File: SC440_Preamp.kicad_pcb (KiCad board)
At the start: 2 copper layers, 30 x 35 mm, 20 parts, among them J1 JST-XH 1x04 TO DIGITAL BOARD, J2 ANALOG BOARD, U1 OPA1678IDR

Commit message: some minor modifications
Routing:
- net /VCC_A: track 34.8 -> 32.4 mm
- net +5V: track 17.0 -> 15.9 mm

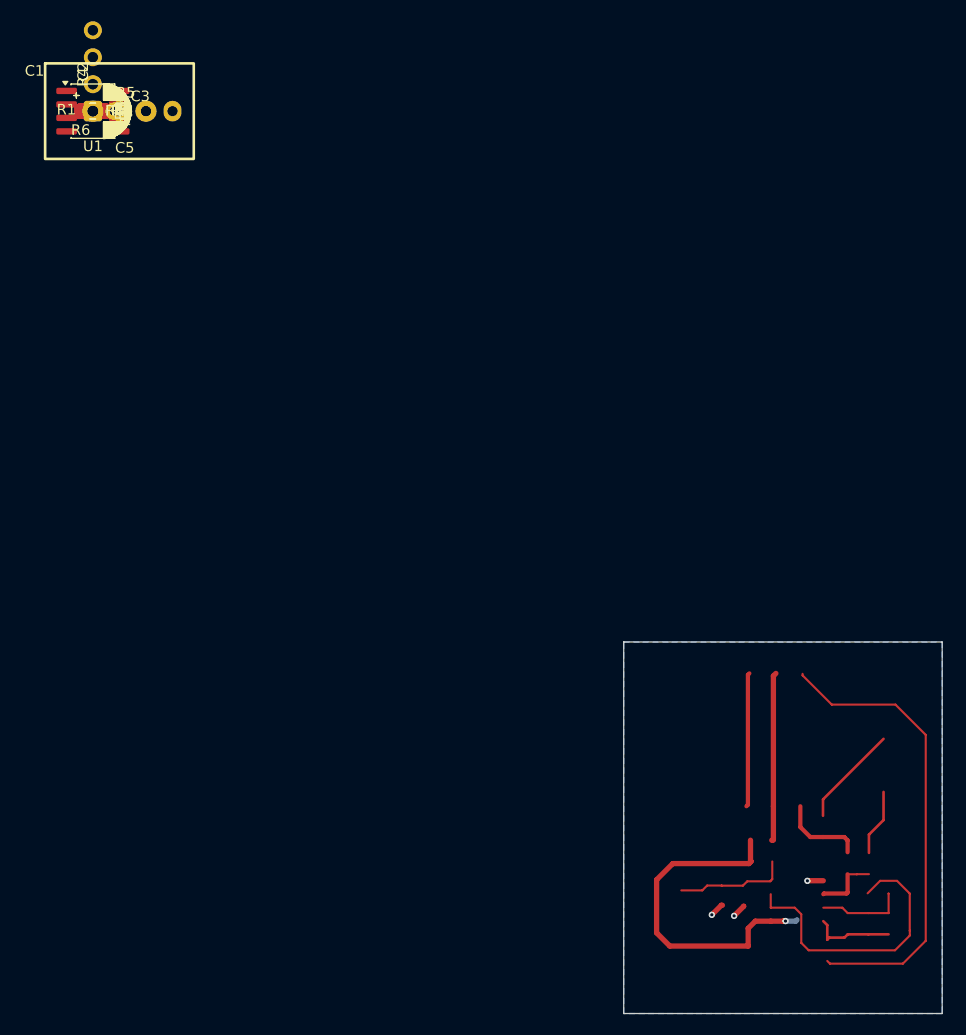
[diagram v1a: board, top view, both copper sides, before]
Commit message: add input and output filter
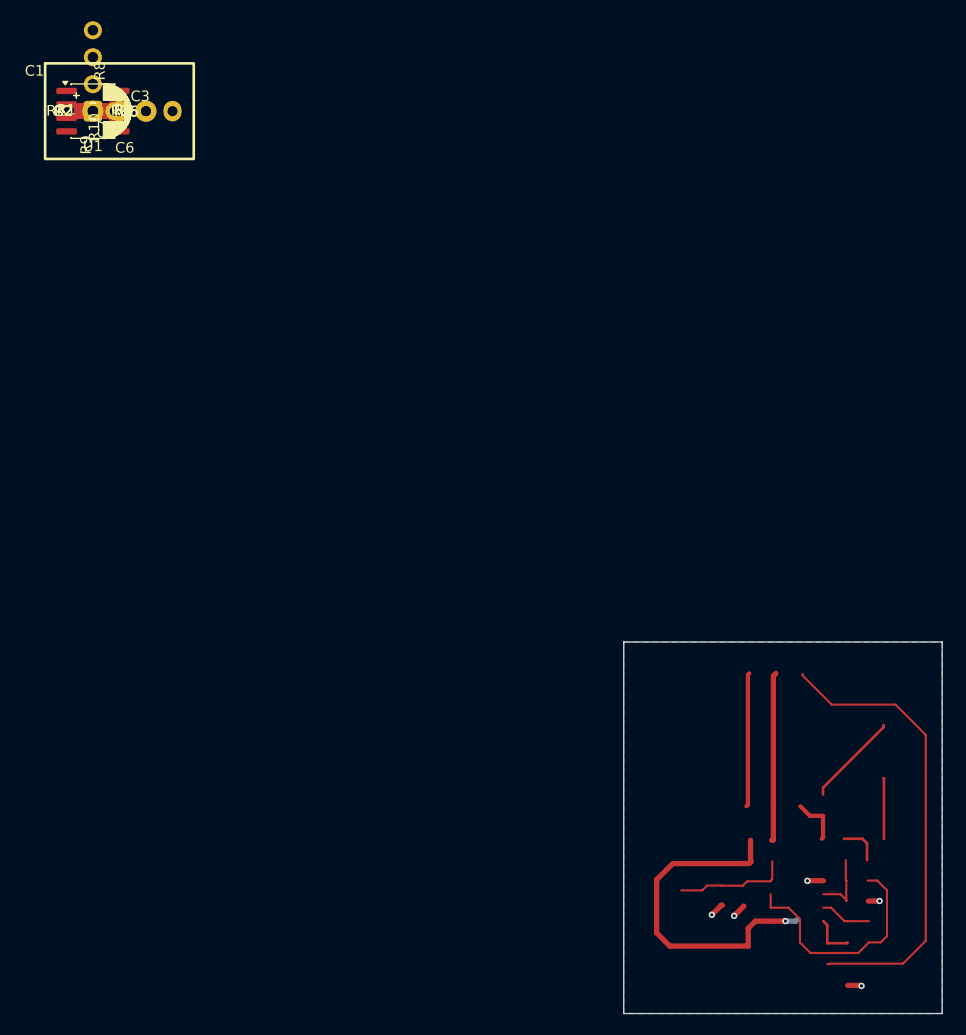
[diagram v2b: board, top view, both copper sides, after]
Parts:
- removed the R8 at (0.00, 0.00)
- removed the R9 at (0.00, 0.00)
- added C5: 330p, Capacitor_SMD:C_0805_2012Metric_Pad1.18x1.45mm_HandSolder, F.Cu at (0.00, 0.00)
- added C7: 1n, Capacitor_SMD:C_0805_2012Metric_Pad1.18x1.45mm_HandSolder, F.Cu at (0.00, 0.00)
- added R4: 1k, Resistor_SMD:R_0805_2012Metric_Pad1.20x1.40mm_HandSolder, F.Cu at (0.00, 0.00)
- renumbered C5 to C6, C6 to C8, R11 to R10, R4 to R2, R2 to R5, R5 to R6, R10 to R8, R6 to R9
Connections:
- C2 pad 2: /IN_AC -> Net-(C2-Pad2)
- R2 pad 2: /IN_AC -> Net-(C2-Pad2)
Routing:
- net /VREF: track 27.1 -> 22.4 mm
- net Net-(C2-Pad2): track 0.00 -> 3.94 mm
- net /PREAMP_OUT: track 7.88 -> 4.19 mm
- net /FB: track 8.20 -> 4.82 mm
- net /ANALOG_INPUT: track 8.05 -> 4.72 mm
- net GND: track 4.16 -> 6.54 mm, vias 3 -> 5
- net Net-(C1-Pad1): track 9.61 -> 8.91 mm
- net Net-(C1-Pad2): track 6.31 -> 5.75 mm

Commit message: add more filtering, silkscreen, pinsockets as spacers
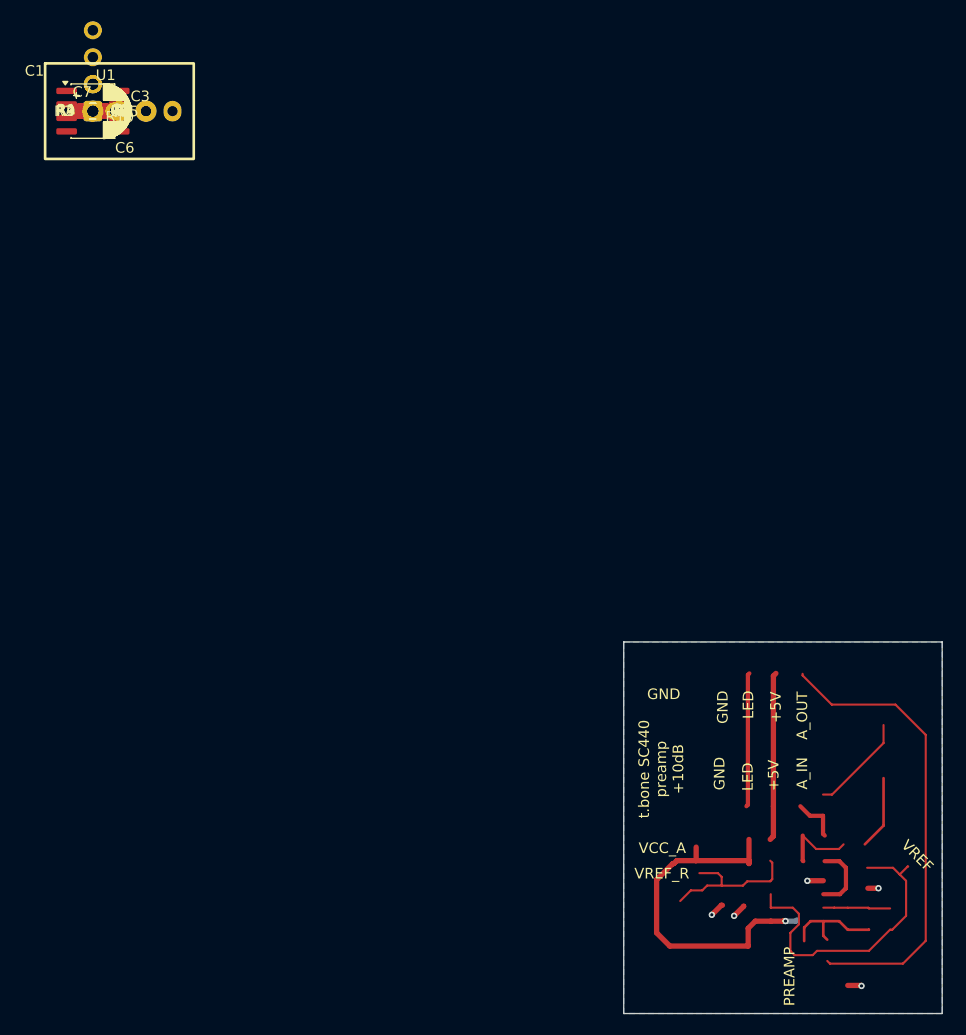
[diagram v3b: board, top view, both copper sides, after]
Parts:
- added C9: 330p, Capacitor_SMD:C_0805_2012Metric_Pad1.18x1.45mm_HandSolder, F.Cu at (0.00, 0.00)
- added REF** (x2): PinSocket_1x02_P2.54mm_Vertical, Connector_PinSocket_2.54mm:PinSocket_1x02_P2.54mm_Vertical, B.Cu at (0.00, 0.00)
- added TP1, TP2, TP3, TP4, TP5: TestPoint, TestPoint:TestPoint_THTPad_1.0x1.0mm_Drill0.5mm, F.Cu at (0.00, 0.00)
- R8: value 22k -> 2.2k
- R9: value 10k -> 1k
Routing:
- net /VREF: track 22.4 -> 29.2 mm
- net /PREAMP_OUT: track 4.19 -> 9.86 mm
- net /VREF_RAW: track 10.7 -> 14.4 mm
- net Net-(C2-Pad2): track 3.94 -> 6.99 mm
- net /FB: track 4.82 -> 6.32 mm
- net /VCC_A: track 32.4 -> 33.8 mm
- net Net-(C1-Pad2): track 5.75 -> 6.97 mm
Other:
- board text added: "PREAMP"
- board text added: "R8 2.2k = 10dB gain R8 1.5k = 8dB gain R8 1.0k = 6db gain"
- board text added: "VCC_A"
- board text added: "VREF"
- board text added: "VREF_R"
- board text added: "t.bone SC440 preamp +10dB"
